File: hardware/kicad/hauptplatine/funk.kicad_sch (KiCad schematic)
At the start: 17 parts, among them U401 Ra-01SH, U402 64 Mbit SOIC-8 208 mil

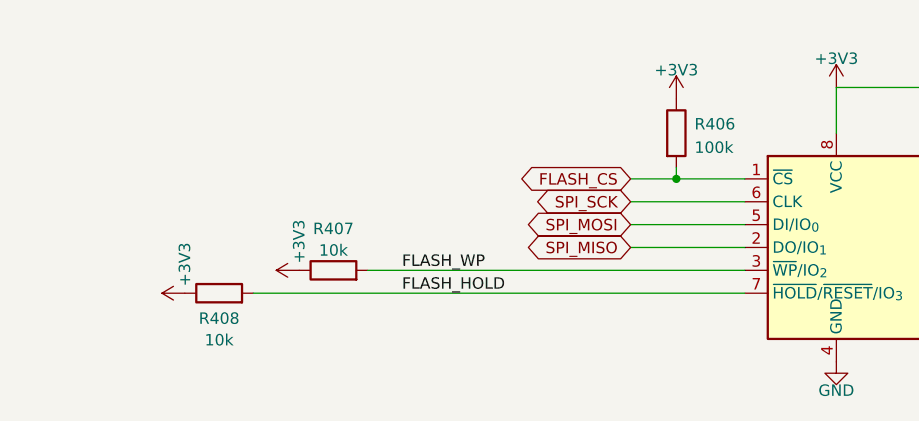
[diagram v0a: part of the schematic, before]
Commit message: HW-11: sechs Bauteile entfallen (R302, C308, FB301, C306, R407, R408), Sanftanlauf R314/C317 am BLE-Lastschalter
Philipp: sichere Streichungen und Sanftanlauf ja, 5-V-Wandler der Waage bleibt. PB2 direkt GND, VBAT ohne
eigenen C, VDDA direkt an +3V3 (C305), Flash WP/HOLD direkt an +3V3; drei begruendete ERC-Warnungen
(pin_to_pin) in erc_erwartet.json. Netzpruefung 237/237, Pin/Footprint 182/0, SPICE 12/12 (S3: 55 mA, 3,29 V).

Co-Authored-By: Claude Fable 5.1 <noreply@anthropic.com>
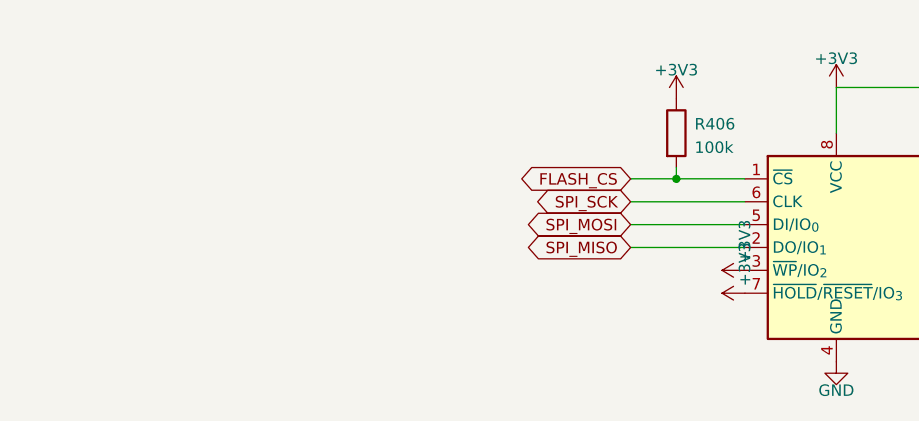
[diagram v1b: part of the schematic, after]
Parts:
- removed R407, R408: 10k, Resistor_SMD:R_0603_1608Metric, symbol Device:R
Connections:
- net FLASH_HOLD is gone; now on net +3V3: U402.7 (~{HOLD}/~{RESET}/IO_{3})
- net FLASH_WP is gone; now on net +3V3: U402.3 (~{WP}/IO_{2})
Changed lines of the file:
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@@
-	(wire
-		(pts
-			(xy 107.95 195.58) (xy 162.56 195.58)
-		)
-		(stroke
-			(width 0)
-			(type default)
-		)
-	)
 	(wire
 		(pts
@@
 		(pts
 			(xy 86.36 124.46) (xy 148.59 124.46)
-		)
-		(stroke
-			(width 0)
-			(type default)
-		)
-	)
-	(wire
-		(pts
-			(xy 120.65 193.04) (xy 162.56 193.04)
 		)
 		(stroke
@@
 		)
 	)
-	(label "FLASH_WP"
-		(at 124.46 193.04 0)
-		(effects
-			(font
-				(size 1.27 1.27)
-			)
-			(justify left bottom)
-		)
-	)
 	(label "RF_MISO"
 		(at 167.64 127 0)
@@
 	(label "RF_SCK"
 		(at 167.64 121.92 0)
-		(effects
-			(font
-				(size 1.27 1.27)
-			)
-			(justify left bottom)
-		)
-	)
-	(label "FLASH_HOLD"
-		(at 124.46 195.58 0)
 		(effects
 			(font
@@
 	(symbol
 		(lib_id "power:+3V3")
-		(at 154.94 173.99 0)
+		(at 162.56 195.58 90)
 		(unit 1)
 		(body_style 1)
@@
 		(dnp no)
 		(property "Reference" "#PWR4011"
-			(at 154.94 173.99 0)
+			(at 162.56 195.58 0)
 			(hide yes)
 			(show_name no)
@@
 		)
 		(property "Value" "+3V3"
-			(at 154.94 170.79 0)
+			(at 162.56 192.38 0)
 			(show_name no)
 			(do_not_autoplace no)
@@
 		)
 		(property "Footprint" ""
-			(at 154.94 173.99 0)
+			(at 162.56 195.58 0)
 			(hide yes)
 			(show_name no)
@@
 		)
 		(property "Datasheet" ""
-			(at 154.94 173.99 0)
+			(at 162.56 195.58 0)
 			(hide yes)
 			(show_name no)
@@
 		)
 		(property "Description" ""
-			(at 154.94 173.99 0)
+			(at 162.56 195.58 0)
 			(show_name no)
 			(do_not_autoplace no)
@@
 	(symbol
 		(lib_id "power:+3V3")
-		(at 100.33 195.58 90)
+		(at 154.94 173.99 0)
 		(unit 1)
 		(body_style 1)
@@
 		(dnp no)
 		(property "Reference" "#PWR4013"
-			(at 100.33 195.58 0)
+			(at 154.94 173.99 0)
 			(hide yes)
 			(show_name no)
@@
 		)
 		(property "Value" "+3V3"
-			(at 100.33 192.38 0)
+			(at 154.94 170.79 0)
 			(show_name no)
 			(do_not_autoplace no)
@@
 		)
 		(property "Footprint" ""
-			(at 100.33 195.58 0)
+			(at 154.94 173.99 0)
 			(hide yes)
 			(show_name no)
@@
 		)
 		(property "Datasheet" ""
-			(at 100.33 195.58 0)
+			(at 154.94 173.99 0)
 			(hide yes)
 			(show_name no)
@@
 		)
 		(property "Description" ""
-			(at 100.33 195.58 0)
+			(at 154.94 173.99 0)
 			(show_name no)
 			(do_not_autoplace no)
@@
 				(path "/69595bfe-3184-5a98-8dcb-39e42f38dc44/24bb1957-0e1d-5b8d-8126-98e840da7728"
 					(reference "#PWR4013")
-					(unit 1)
-				)
-			)
-		)
-	)
-	(symbol
-		(lib_id "Device:R")
-		(at 116.84 193.04 90)
-		(unit 1)
-		(body_style 1)
-		(exclude_from_sim no)
-		(in_bom yes)
-		(on_board yes)
-		(in_pos_files yes)
-		(dnp no)
-		(property "Reference" "R407"
-			(at 116.84 188.424 90)
-			(show_name no)
-			(do_not_autoplace no)
-			(effects
-				(font
-					(size 1.27 1.27)
-				)
-			)
-		)
-		(property "Value" "10k"
-			(at 116.84 190.824 90)
-			(show_name no)
-			(do_not_autoplace no)
-			(effects
-				(font
-					(size 1.27 1.27)
-				)
-			)
-		)
-		(property "Footprint" "Resistor_SMD:R_0603_1608Metric"
-			(at 116.84 193.04 0)
-			(hide yes)
-			(show_name no)
-			(do_not_autoplace no)
-			(effects
-				(font
-					(size 1.27 1.27)
-				)
-			)
-		)
-		(property "Datasheet" ""
-			(at 116.84 193.04 0)
-			(hide yes)
-			(show_name no)
-			(do_not_autoplace no)
-			(effects
-				(font
-					(size 1.27 1.27)
-				)
-			)
-		)
-		(property "Description" ""
-			(at 116.84 193.04 0)
-			(hide yes)
-			(show_name no)
-			(do_not_autoplace no)
-			(effects
-				(font
-					(size 1.27 1.27)
-				)
-			)
-		)
-		(pin "1"
-		)
-		(pin "2"
-		)
-		(instances
-			(project "logger"
-				(path "/69595bfe-3184-5a98-8dcb-39e42f38dc44/24bb1957-0e1d-5b8d-8126-98e840da7728"
-					(reference "R407")
 					(unit 1)
 				)
@@
 	)
 	(symbol
-		(lib_id "power:+3V3")
-		(at 113.03 193.04 90)
+		(lib_id "power:GND")
+		(at 185.42 180.34 0)
 		(unit 1)
 		(body_style 1)
@@
 		(dnp no)
 		(property "Reference" "#PWR4012"
-			(at 113.03 193.04 0)
-			(hide yes)
-			(show_name no)
-			(do_not_autoplace no)
-			(effects
-				(font
-					(size 1.27 1.27)
-				)
-			)
-		)
-		(property "Value" "+3V3"
-			(at 113.03 189.84 0)
+			(at 185.42 180.34 0)
+			(hide yes)
+			(show_name no)
+			(do_not_autoplace no)
+			(effects
+				(font
+					(size 1.27 1.27)
+				)
+			)
+		)
+		(property "Value" "GND"
+			(at 185.42 183.54 0)
 			(show_name no)
 			(do_not_autoplace no)
@@
 		)
 		(property "Footprint" ""
-			(at 113.03 193.04 0)
+			(at 185.42 180.34 0)
 			(hide yes)
 			(show_name no)
@@
 		)
 		(property "Datasheet" ""
-			(at 113.03 193.04 0)
+			(at 185.42 180.34 0)
 			(hide yes)
 			(show_name no)
@@
 		)
 		(property "Description" ""
-			(at 113.03 193.04 0)
+			(at 185.42 180.34 0)
 			(show_name no)
 			(do_not_autoplace no)
@@
 	)
 	(symbol
-		(lib_id "power:GND")
-		(at 172.72 203.2 0)
+		(lib_id "power:+3V3")
+		(at 162.56 193.04 90)
 		(unit 1)
 		(body_style 1)
@@
 		(dnp no)
 		(property "Reference" "#PWR4009"
-			(at 172.72 203.2 0)
-			(hide yes)
-			(show_name no)
-			(do_not_autoplace no)
-			(effects
-				(font
-					(size 1.27 1.27)
-				)
-			)
-		)
-		(property "Value" "GND"
-			(at 172.72 206.4 0)
+			(at 162.56 193.04 0)
+			(hide yes)
+			(show_name no)
+			(do_not_autoplace no)
+			(effects
+				(font
+					(size 1.27 1.27)
+				)
+			)
+		)
+		(property "Value" "+3V3"
+			(at 162.56 189.84 0)
 			(show_name no)
 			(do_not_autoplace no)
@@
 		)
 		(property "Footprint" ""
-			(at 172.72 203.2 0)
+			(at 162.56 193.04 0)
 			(hide yes)
 			(show_name no)
@@
 		)
 		(property "Datasheet" ""
-			(at 172.72 203.2 0)
+			(at 162.56 193.04 0)
 			(hide yes)
 			(show_name no)
@@
 		)
 		(property "Description" ""
-			(at 172.72 203.2 0)
+			(at 162.56 193.04 0)
 			(show_name no)
 			(do_not_autoplace no)
@@
 	(symbol
 		(lib_id "Device:R")
-		(at 104.14 195.58 90)
-		(unit 1)
-		(body_style 1)
-		(exclude_from_sim no)
-		(in_bom yes)
-		(on_board yes)
-		(in_pos_files yes)
-		(dnp no)
-		(property "Reference" "R408"
-			(at 104.14 198.396 90)
-			(show_name no)
-			(do_not_autoplace no)
-			(effects
-				(font
-					(size 1.27 1.27)
-				)
-			)
-		)
-		(property "Value" "10k"
-			(at 104.14 200.796 90)
-			(show_name no)
-			(do_not_autoplace no)
-			(effects
-				(font
-					(size 1.27 1.27)
-				)
-			)
-		)
-		(property "Footprint" "Resistor_SMD:R_0603_1608Metric"
-			(at 104.14 195.58 0)
-			(hide yes)
-			(show_name no)
-			(do_not_autoplace no)
-			(effects
-				(font
-					(size 1.27 1.27)
-				)
-			)
-		)
-		(property "Datasheet" ""
-			(at 104.14 195.58 0)
-			(hide yes)
-			(show_name no)
-			(do_not_autoplace no)
-			(effects
-				(font
-					(size 1.27 1.27)
-				)
-			)
-		)
-		(property "Description" ""
-			(at 104.14 195.58 0)
-			(hide yes)
-			(show_name no)
-			(do_not_autoplace no)
-			(effects
-				(font
-					(size 1.27 1.27)
-				)
-			)
-		)
-		(pin "1"
-		)
-		(pin "2"
-		)
-		(instances
-			(project "logger"
-				(path "/69595bfe-3184-5a98-8dcb-39e42f38dc44/24bb1957-0e1d-5b8d-8126-98e840da7728"
-					(reference "R408")
-					(unit 1)
-				)
-			)
-		)
-	)
-	(symbol
-		(lib_id "Device:R")
 		(at 152.4 119.38 90)
 		(unit 1)
@@
 	(symbol
 		(lib_id "power:GND")
-		(at 185.42 180.34 0)
+		(at 172.72 203.2 0)
 		(unit 1)
 		(body_style 1)
@@
 		(dnp no)
 		(property "Reference" "#PWR4010"
-			(at 185.42 180.34 0)
+			(at 172.72 203.2 0)
 			(hide yes)
 			(show_name no)
@@
 		)
 		(property "Value" "GND"
-			(at 185.42 183.54 0)
+			(at 172.72 206.4 0)
 			(show_name no)
 			(do_not_autoplace no)
@@
 		)
 		(property "Footprint" ""
-			(at 185.42 180.34 0)
+			(at 172.72 203.2 0)
 			(hide yes)
 			(show_name no)
@@
 		)
 		(property "Datasheet" ""
-			(at 185.42 180.34 0)
+			(at 172.72 203.2 0)
 			(hide yes)
 			(show_name no)
@@
 		)
 		(property "Description" ""
-			(at 185.42 180.34 0)
-			(show_name no)
-			(do_not_autoplace no)
+			(at 172.72 203.2 0)
+			(show_name no)
+			(do_not_autoplace no)
